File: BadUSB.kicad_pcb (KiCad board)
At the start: 2 copper layers, 43.7 x 24.4 mm, 17 parts, among them J1 USB_A, J2 Conn_01x06_Pin, U1 PIC12F1840-xSN, U2 24AA02-OT

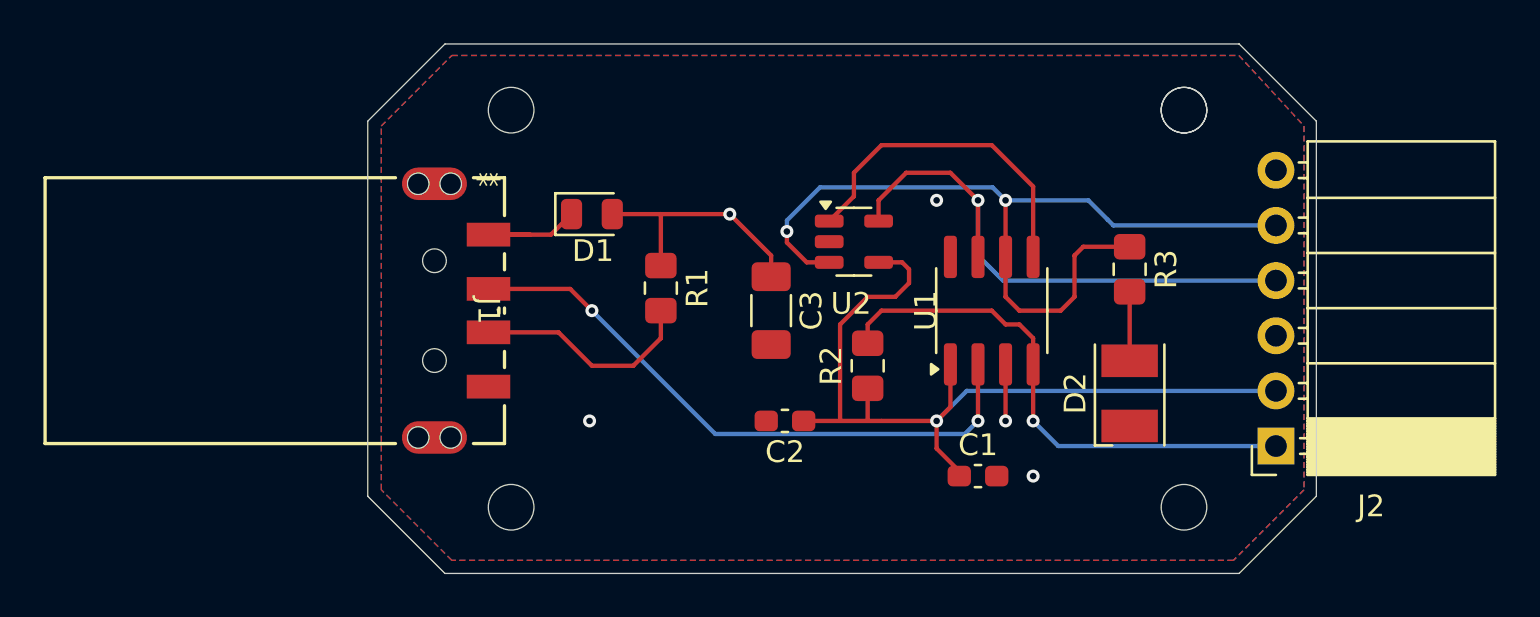
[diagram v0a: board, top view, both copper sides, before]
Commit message: cleaned up traces and fix silkscreen
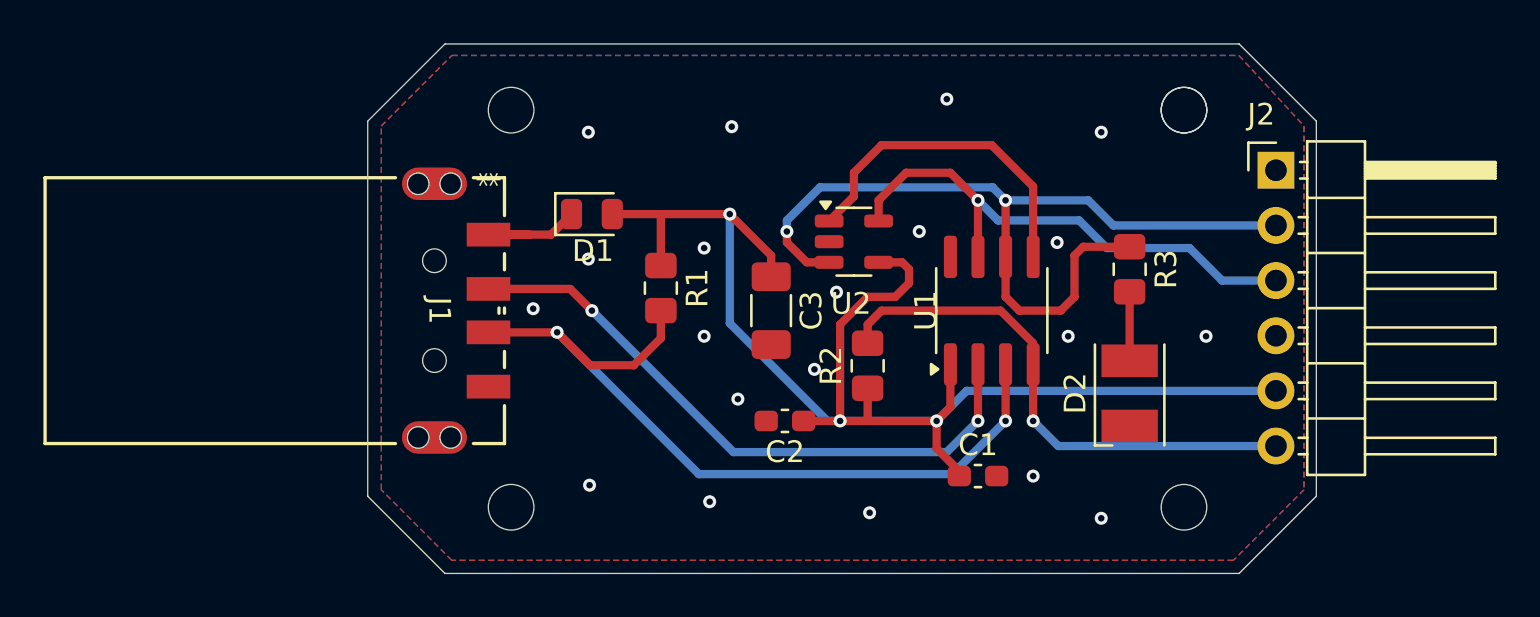
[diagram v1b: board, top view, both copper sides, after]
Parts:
- J2: footprint Connector_PinSocket_2.54mm:PinSocket_1x06_P2.54mm_Horizontal -> Connector_PinHeader_2.54mm:PinHeader_1x06_P2.54mm_Horizontal
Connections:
- D1 pad 2: Net-(D1-A) -> VDD
- J1 pad 1: Net-(D1-A) -> VDD
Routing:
- net D+: track 13.0 -> 37.3 mm, vias 1 -> 2
- net VDD: track 51.7 -> 74.2 mm, vias 2 -> 3
- net Net-(D1-A): track 6.13 -> 0.00 mm
- net PGD: track 25.9 -> 24.4 mm
- net D-: track 28.2 -> 28.9 mm
- net GND: vias 3 -> 20
